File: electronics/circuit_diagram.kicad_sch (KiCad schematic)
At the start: 12 parts, among them M1 base_motor, M2 shoulder_motor, M3 elbow_motor, M4 wrist_motor, M5 gripper_motor, P1 base_potentiometer, P2 shoulder_potentiometer, P3 elbow_potentiometer, P4 wrist_potentiometer, P5 gripper_potentiometer

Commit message: added mode switching button and feedback LED
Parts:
- added B1: mode_switching_button, symbol Switch:SW_Push
- added L1: feedback_led, symbol Device:LED
- added R1: 220Ω, symbol Device:R
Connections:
- net at A1.7 (GND), M1.3 (-), M2.3 (-)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: now also B1.2, L1.1 (K)
- net at A1.17 (D2): now also B1.1
- net at A1.19 (D4): now also R1.1
- new net: L1.2 (A), R1.2

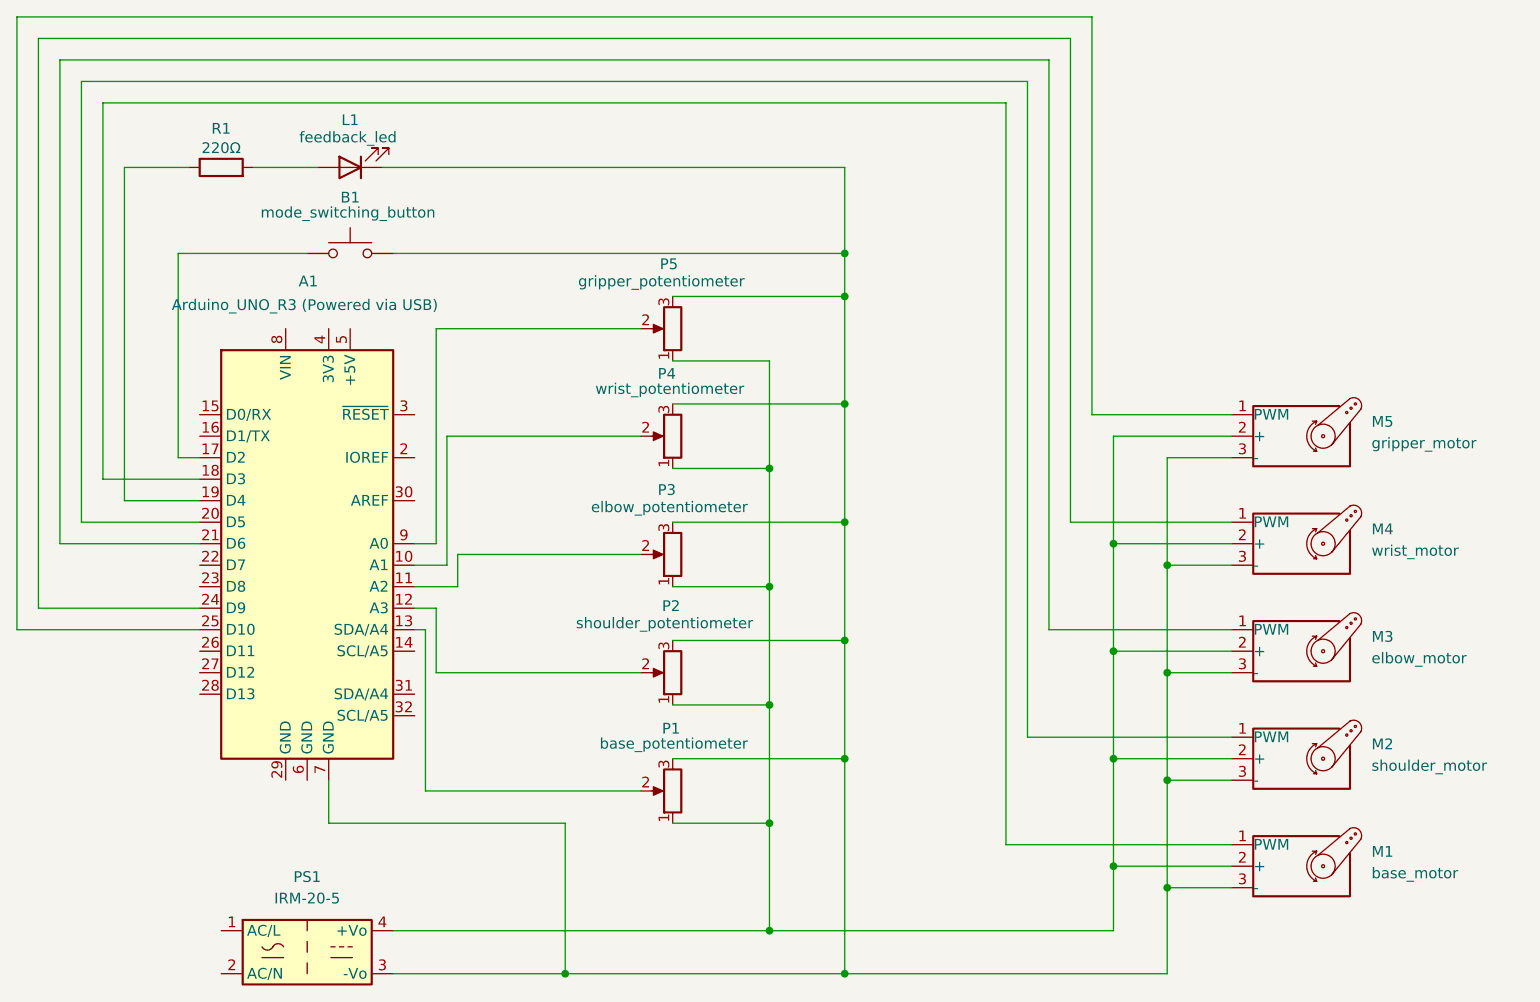
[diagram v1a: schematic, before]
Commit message: fixed potentiometer supply: use Arduino 5V instead of external power
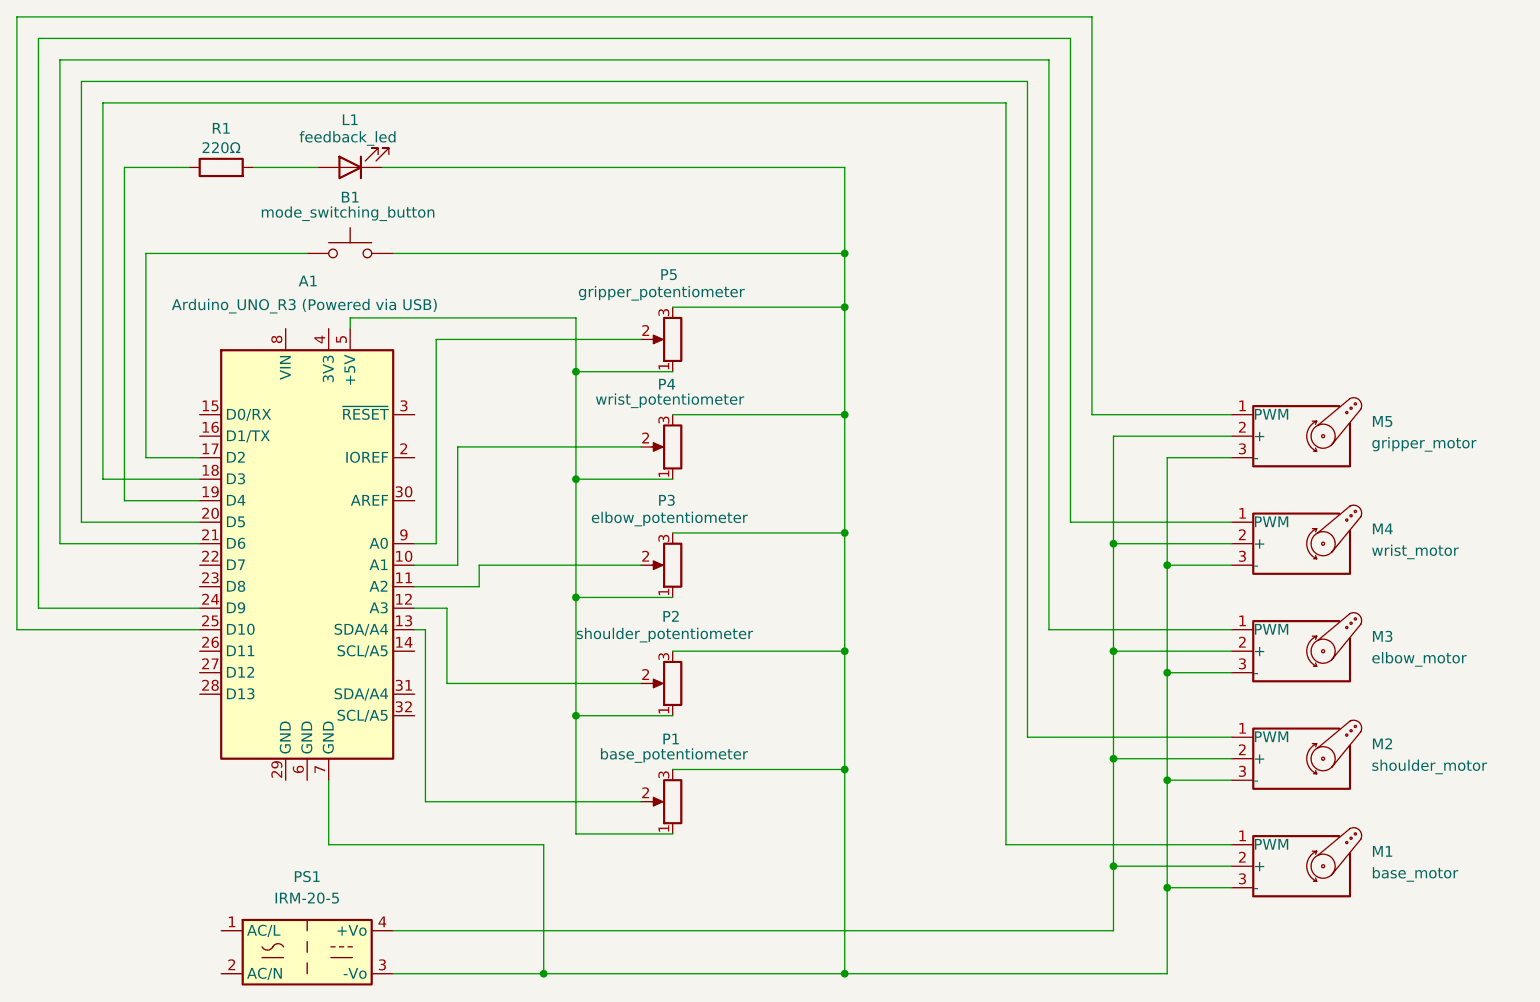
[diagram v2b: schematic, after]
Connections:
- net at M1.2 (+), M2.2 (+), M3.2 (+)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: no longer P1.1, P2.1, P3.1, P4.1, P5.1
- net at A1.5 (+5V): now also P1.1, P2.1, P3.1, P4.1, P5.1
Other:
- moved on the sheet: P1, P2, P3, P4, P5
